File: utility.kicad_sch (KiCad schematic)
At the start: 28 parts, among them J12 Raspberry Pi Power/UART, J7 Extra 12V, J8 Extra 12V

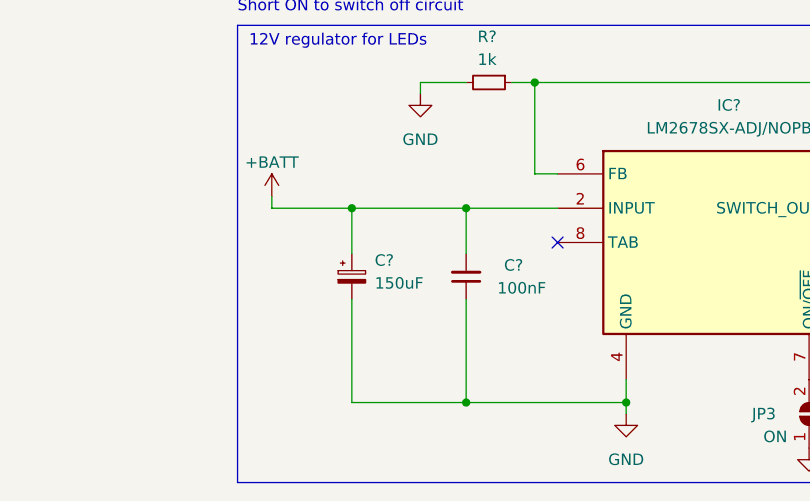
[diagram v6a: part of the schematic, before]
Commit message: completed 12 V regulators routing
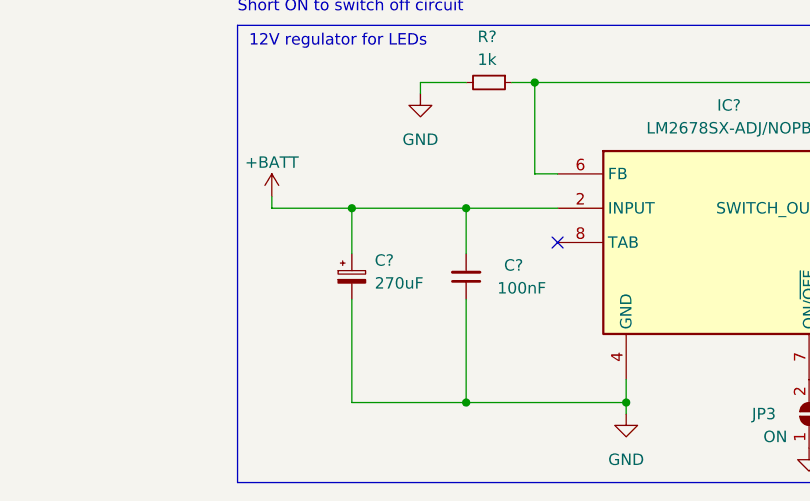
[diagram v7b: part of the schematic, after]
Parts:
- C?: value 150uF -> 270uF; footprint SamacSys_Parts:EEHZT1E331UP -> SamacSys_Parts:EEHZS1H221P
- IC?: footprint SamacSys_Parts:KTW0007B -> rbc Custom Library:KTW0007B_custom
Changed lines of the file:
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@@
       (effects (font (size 1.27 1.27)) (justify left))
     )
-    (property "Value" "150uF" (at 88.9 127.7239 0)
+    (property "Value" "270uF" (at 88.9 127.7239 0)
       (effects (font (size 1.27 1.27)) (justify left))
     )
-    (property "Footprint" "SamacSys_Parts:EEHZT1E331UP" (at 86.36 127 0)
+    (property "Footprint" "SamacSys_Parts:EEHZS1H221P" (at 86.36 127 0)
       (effects (font (size 1.27 1.27)) hide)
     )
@@
       (effects (font (size 1.27 1.27)))
     )
-    (property "Footprint" "SamacSys_Parts:KTW0007B" (at 143.51 210.49 0)
+    (property "Footprint" "rbc Custom Library:KTW0007B_custom" (at 143.51 210.49 0)
       (effects (font (size 1.27 1.27)) (justify left top) hide)
     )
